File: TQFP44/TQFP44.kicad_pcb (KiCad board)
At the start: 2 copper layers, 56.4 x 20.8 mm, 7 parts, among them J1 Conn_01x22, J2 Conn_01x22, J3 Conn_02x22_Counter_Clockwise, J4 Conn_02x22_Counter_Clockwise

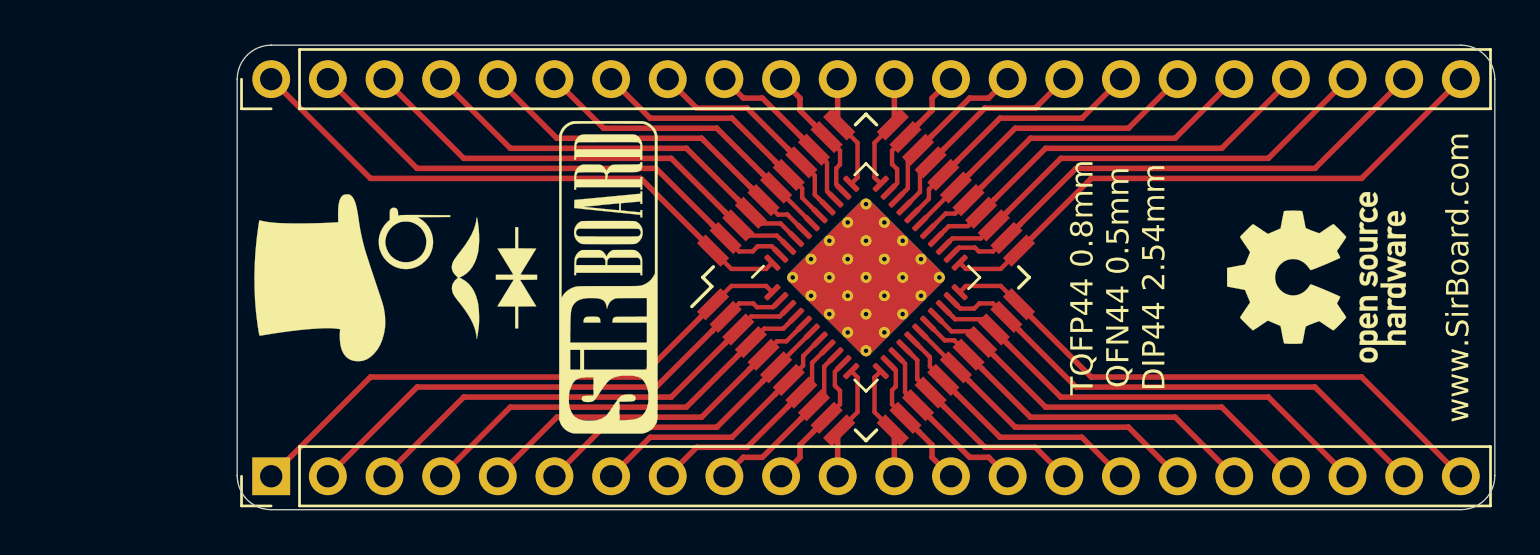
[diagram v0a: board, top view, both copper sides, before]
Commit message: SOIC20 and SOIC28 Added
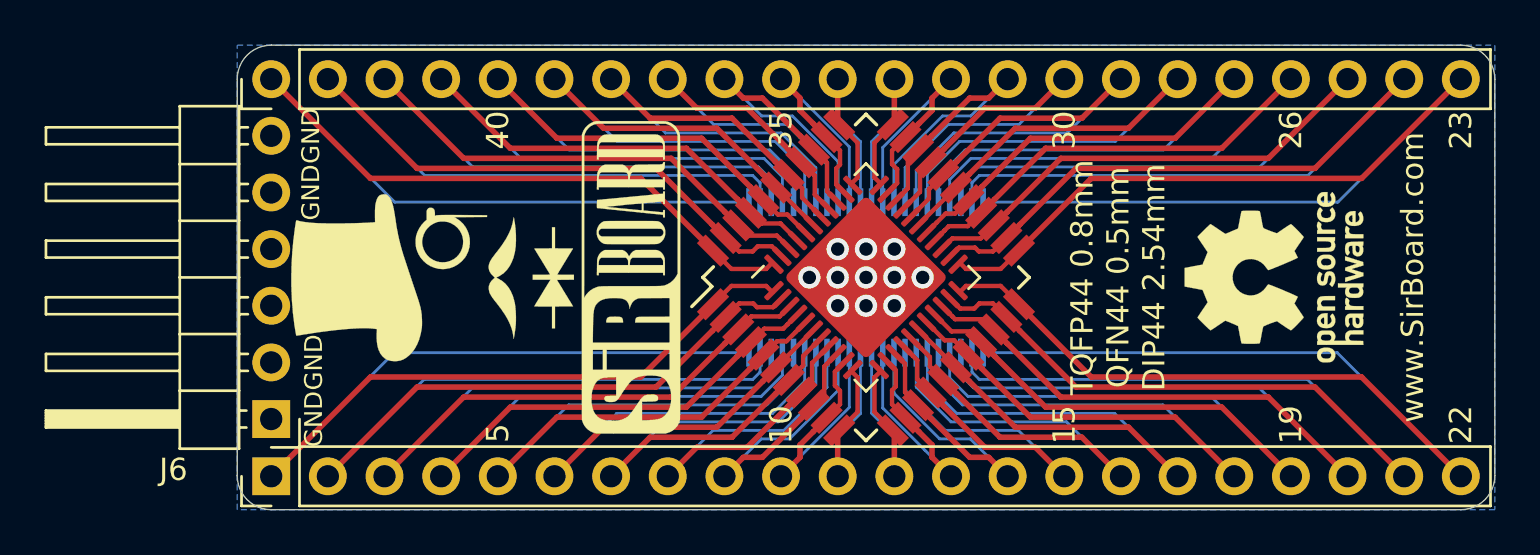
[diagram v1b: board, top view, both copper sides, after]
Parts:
- added G***: LOGO, logo:logo126x178, B.Cu at (215.6, 72.4)
- added G***: LOGO, logo:SirBoard140x44, B.Cu at (205.9, 72.3)
- added J5: Conn_02x22_Counter_Clockwise, Package_SO:SSOP-44_5.3x12.8mm_P0.5mm, B.Cu at (194.4, 72.4)
- added J6: Conn_01x06, Connector_PinHeader_2.54mm:PinHeader_1x06_P2.54mm_Horizontal, F.Cu at (167.8, 78.7)
- added REF**: OSHW-Logo_7.5x8mm_SilkScreen, Symbol:OSHW-Logo_7.5x8mm_SilkScreen, B.Cu at (177.2, 72.4)
- J4: value Conn_02x22_Counter_Clockwise -> Conn_02x22_Counter_Clockwise_MountingPin; footprint Package_DFN_QFN:QFN-44-1EP_7x7mm_P0.5mm_EP5.15x5.15mm_ThermalVias -> Package_DFN_QFN:QFN-44-1EP_7x7mm_P0.5mm_EP5.2x5.2mm
- moved REF** 1.91 mm to (212.7, 72.4)
- moved G*** 1.65 mm to (175.0, 72.4)
- moved G*** 1.02 mm to (183.9, 72.4)
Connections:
- J4 pad 45: (no net) -> Net-(J4-PadMP)
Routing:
- net Net-(J1-Pad1): track 26.1 -> 49.8 mm
- net Net-(J2-Pad22): track 26.1 -> 49.8 mm
- net Net-(J2-Pad1): track 26.1 -> 49.8 mm
- net Net-(J1-Pad22): track 26.1 -> 49.8 mm
- net Net-(J1-Pad2): track 23.7 -> 45.9 mm
- net Net-(J2-Pad21): track 23.7 -> 45.9 mm
- net Net-(J2-Pad2): track 23.7 -> 45.9 mm
- net Net-(J1-Pad21): track 23.7 -> 45.9 mm
- net Net-(J1-Pad3): track 21.2 -> 41.4 mm
- net Net-(J2-Pad20): track 21.2 -> 41.4 mm
- net Net-(J2-Pad3): track 21.2 -> 41.4 mm
- net Net-(J1-Pad20): track 21.2 -> 41.4 mm
- net Net-(J1-Pad4): track 18.9 -> 37.1 mm
- net Net-(J2-Pad19): track 18.9 -> 37.1 mm
- net Net-(J2-Pad4): track 18.9 -> 37.1 mm
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- added copper zone on B.Cu, net Net-(J4-PadMP)
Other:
- net class Default: clearance 0.2 -> 0.127; trace_width 0.25 -> 0.127
- rule trace_clearance: 0.2 -> 0.127
- rule trace_min: 0.2 -> 0.127
- board text added: "10"
- board text added: "15"
- board text added: "19"
- board text added: "22"
- board text added: "23"
- board text added: "26"
- board text added: "30"
- board text added: "35"
- board text added: "40"
- board text added: "5"
- board text added: "GND"
- board text added: "TSSOP 0.5mm DIP44 2.54mm"

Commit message: TQFP/QFN48 Added
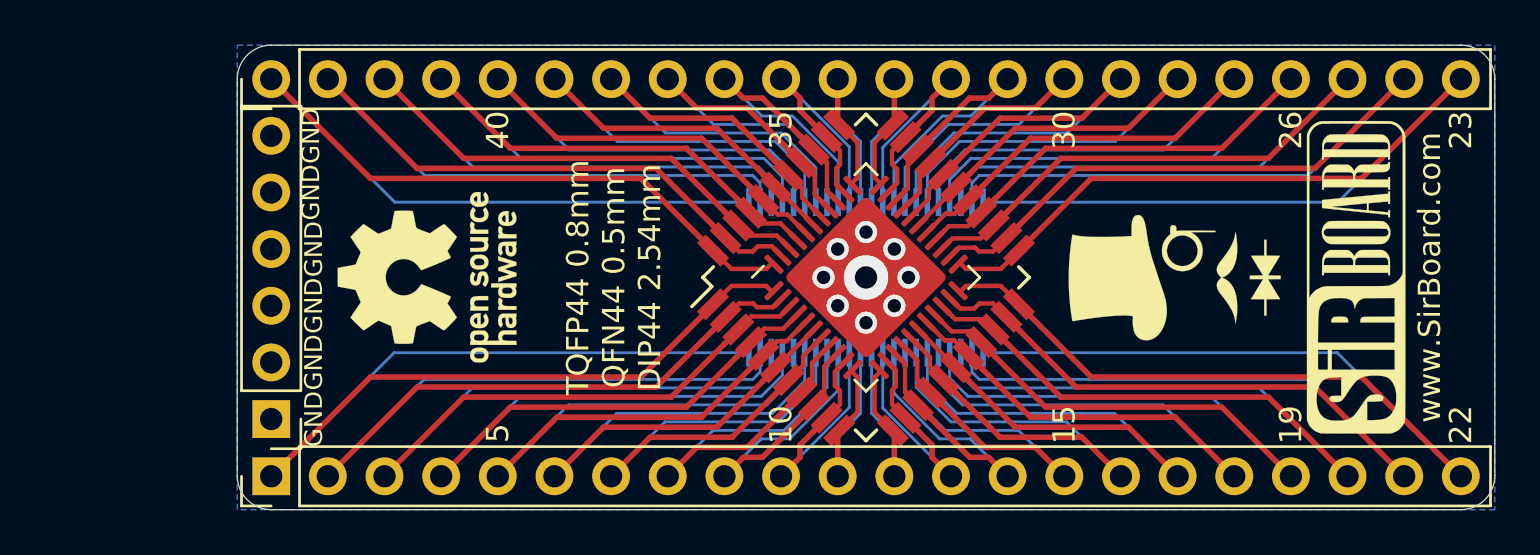
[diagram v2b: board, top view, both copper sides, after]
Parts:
- removed the G*** at (175.0, 72.4)
- added G***: LOGO, logo:logo94x134, F.Cu at (208.3, 72.4)
- J6: footprint Connector_PinHeader_2.54mm:PinHeader_1x06_P2.54mm_Horizontal -> Connector_PinHeader_2.54mm:PinHeader_1x06_P2.54mm_Vertical
- moved REF** 38.0 mm to (174.8, 72.4)
- moved G*** 32.5 mm to (216.4, 72.4)
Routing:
- net Net-(J4-PadMP): vias 11 -> 9

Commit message: Silkscreens and sizes updated
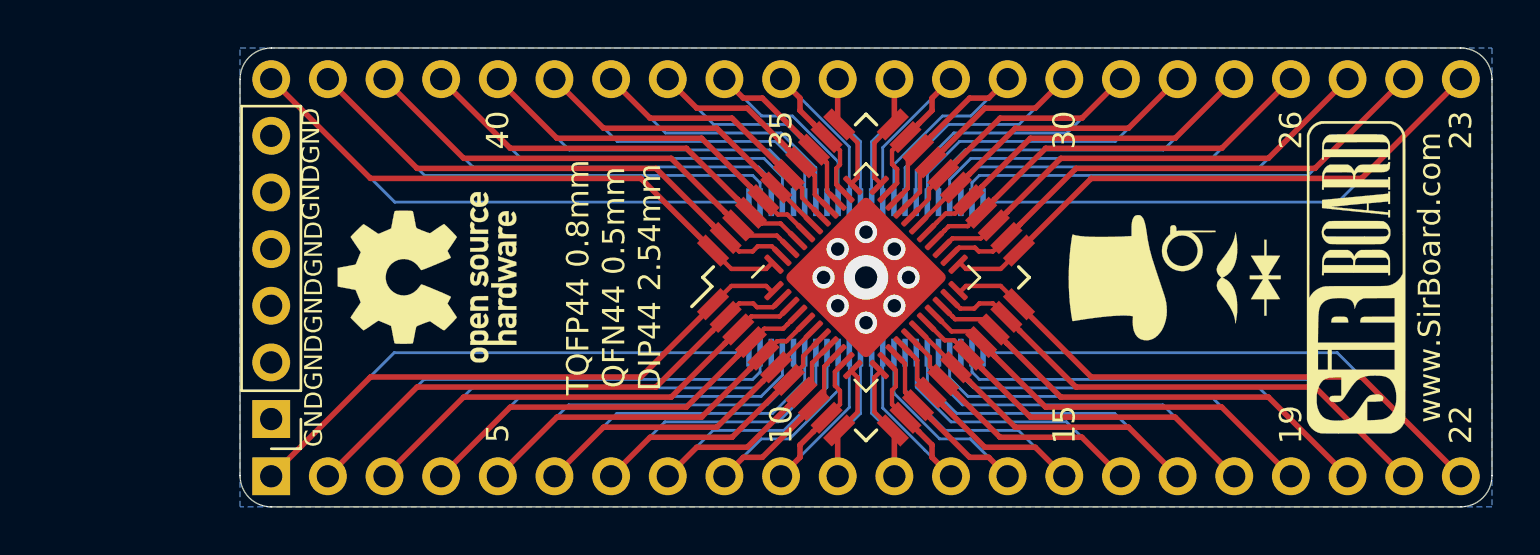
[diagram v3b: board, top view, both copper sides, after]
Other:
- board size 56.4 x 20.8 mm -> 56.1 x 20.6 mm

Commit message: Final Revisions
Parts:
- J4: value Conn_02x22_Counter_Clockwise_MountingPin -> Conn_02x22_Counter_Clockwise; footprint Package_DFN_QFN:QFN-44-1EP_7x7mm_P0.5mm_EP5.2x5.2mm -> Package_DFN_QFN:QFN-44-1EP_7x7mm_P0.5mm_EP5.15x5.15mm
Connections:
- J4 pad 45: Net-(J4-PadMP) -> (no net)
- J6 pad 1: Net-(J4-PadMP) -> Net-(J6-Pad1)
- J6 pad 2: Net-(J4-PadMP) -> Net-(J6-Pad1)
- J6 pad 3: Net-(J4-PadMP) -> Net-(J6-Pad1)
- J6 pad 4: Net-(J4-PadMP) -> Net-(J6-Pad1)
- J6 pad 5: Net-(J4-PadMP) -> Net-(J6-Pad1)
- J6 pad 6: Net-(J4-PadMP) -> Net-(J6-Pad1)
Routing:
- net Net-(J2-Pad9): track 2.64 -> 16.4 mm
- net Net-(J1-Pad14): track 30.0 -> 16.3 mm
- net Net-(J2-Pad10): track 2.95 -> 13.2 mm
- net Net-(J1-Pad13): track 23.4 -> 13.2 mm
- net Net-(J1-Pad9): track 7.96 -> 16.4 mm
- net Net-(J2-Pad14): track 24.9 -> 16.4 mm
- net Net-(J2-Pad13): track 20.0 -> 13.1 mm
- net Net-(J1-Pad10): track 6.34 -> 13.1 mm
- net Net-(J4-PadMP): vias 9 -> 0
- net (no net): vias 0 -> 9
- added copper zone on B.Cu, net Net-(J6-Pad1)
- removed copper zone on B.Cu, net Net-(J4-PadMP)

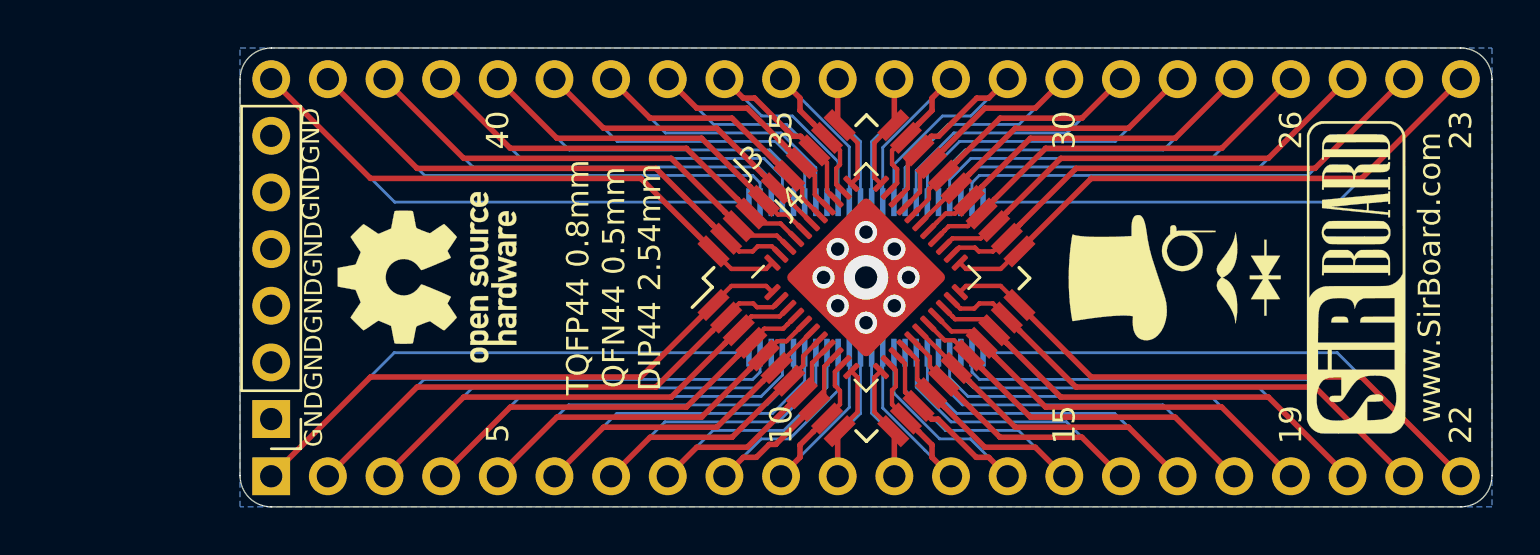
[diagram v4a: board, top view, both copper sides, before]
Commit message: Dimensions Added And TQFP64 Added
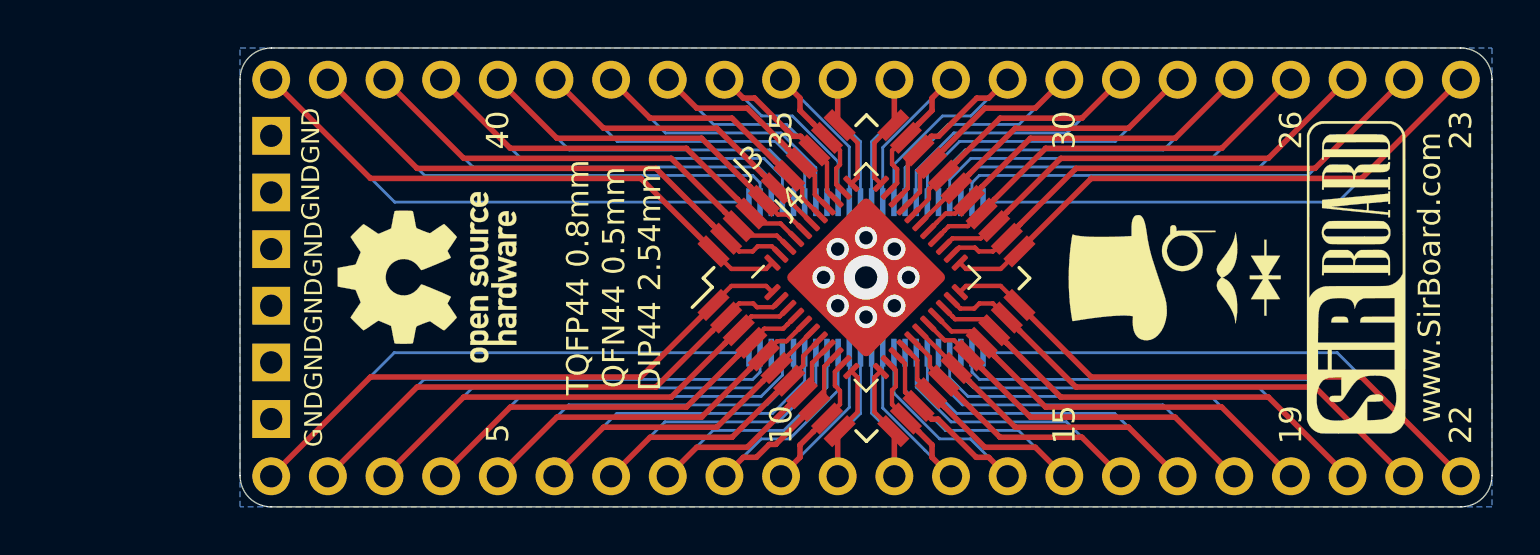
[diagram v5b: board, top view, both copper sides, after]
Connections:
- J4 pad 45: (no net) -> Net-(J6-Pad1)
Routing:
- net Net-(J6-Pad1): vias 0 -> 9
- net (no net): vias 9 -> 0

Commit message: Pin Numbering edited
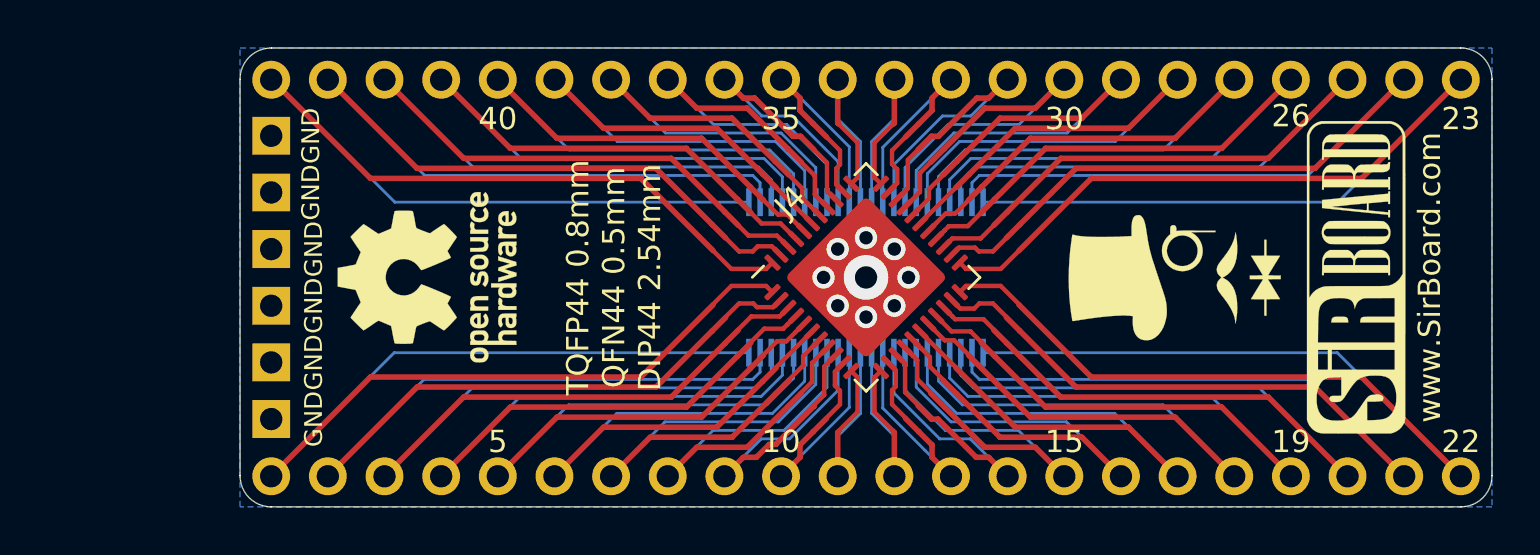
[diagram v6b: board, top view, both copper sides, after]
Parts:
- removed J3: Conn_02x22_Counter_Clockwise, Package_QFP:TQFP-44_10x10mm_P0.8mm
- J1, J2: moved to B.Cu
- turned J1 to 270 degrees
- turned J2 to 270 degrees
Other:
- board text added: "1"
- board text added: "44"

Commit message: Numbering Orientation Edited
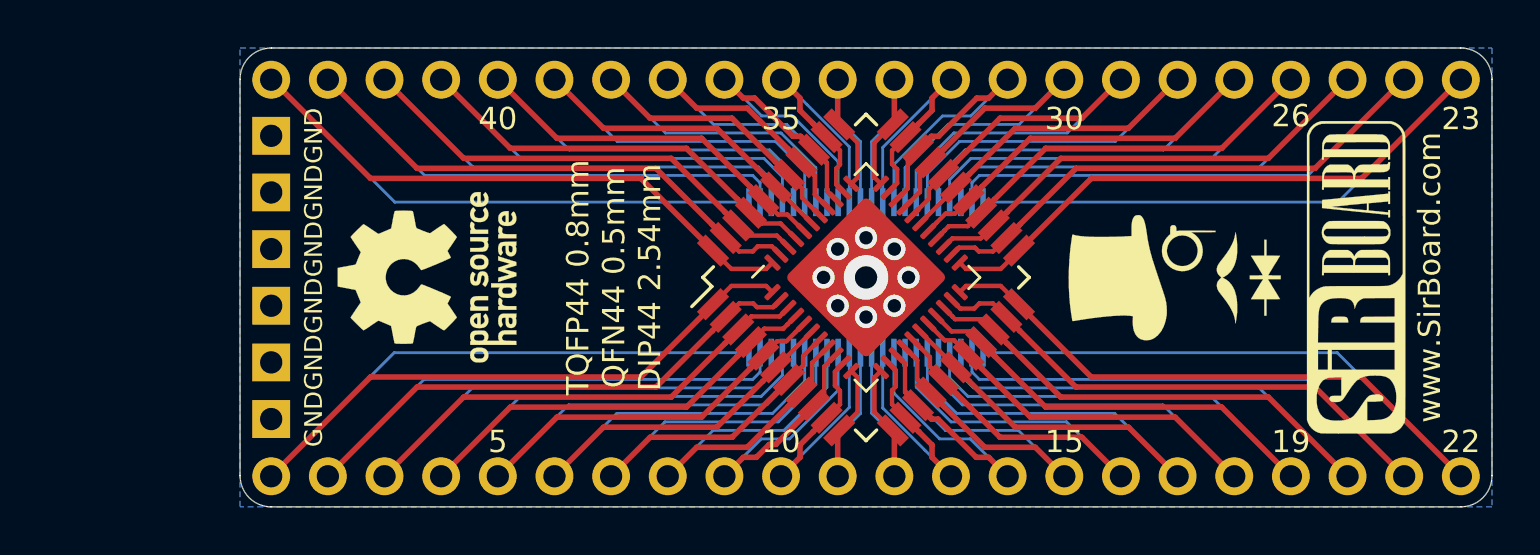
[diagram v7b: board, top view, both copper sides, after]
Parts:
- added J3: Conn_02x22_Counter_Clockwise, Package_QFP:TQFP-44_10x10mm_P0.8mm, F.Cu at (194.4, 72.4)
- J1, J2: moved to F.Cu
- J6: moved to B.Cu
- turned J1 to 90 degrees
- turned J2 to 90 degrees
- turned J6 to 0 degrees
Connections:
- J4 pad 45: Net-(J6-Pad1) -> (no net)
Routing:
- net Net-(J6-Pad1): vias 9 -> 0
- net (no net): vias 0 -> 9
